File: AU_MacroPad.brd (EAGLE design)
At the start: 59.7 x 104.1 mm, 96 parts, among them IC1 74HCT1G125DBV, IC3 RP2040_QFN56, SW2 RA SW, SW3 EN11-VSM1AF15, U1 W25Q64, U2 RT9080-3.3, U3 PAM8302, X1 TYPE C, X2 ZJY130-2864KSWLG22, Y1 12MHz/12pF

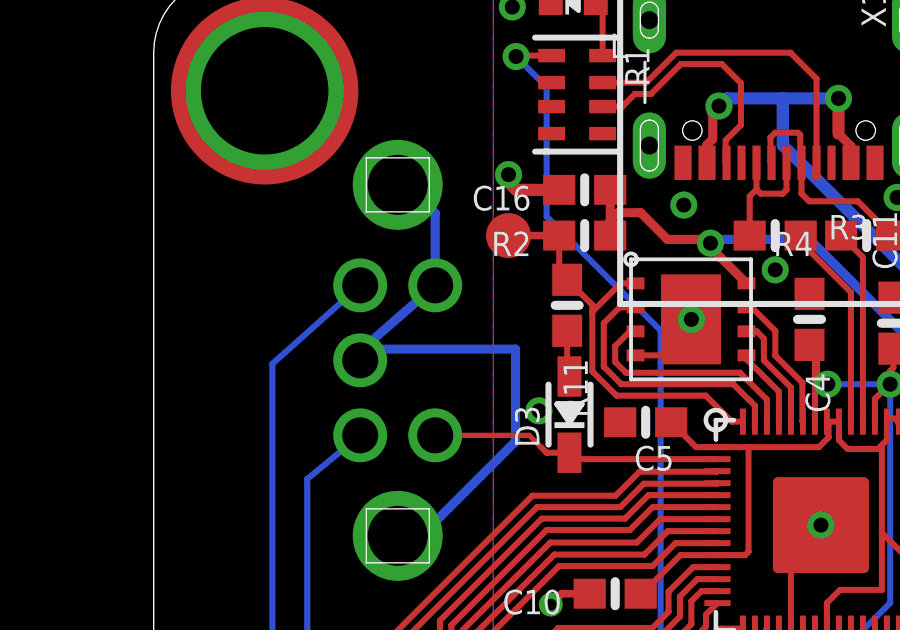
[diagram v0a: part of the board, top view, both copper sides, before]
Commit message: swap gnd and usbboot to match original macropad
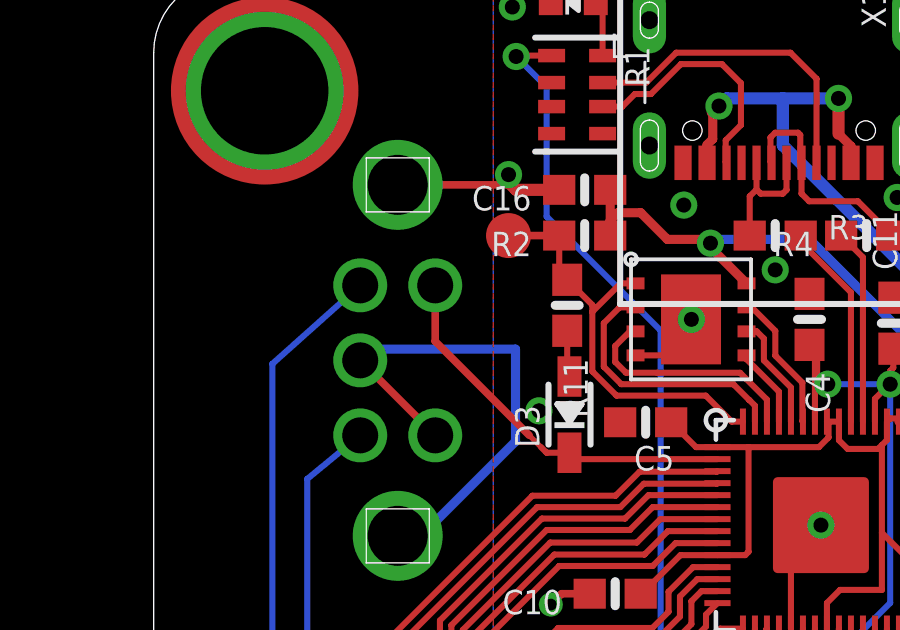
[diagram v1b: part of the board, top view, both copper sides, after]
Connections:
- net GND: now also SW3.D; no longer SW3.E
- net USBBOOT: now also SW3.E; no longer SW3.D
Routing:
- net USBBOOT: track 9.84 -> 13.0 mm
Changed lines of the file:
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@@
 <via x="51.308" y="79.121" extent="1-16" drill="0.5"/>
 <via x="36.114896875" y="96.474196875" extent="1-16" drill="0.5"/>
-<contactref element="SW3" pad="E"/>
 <contactref element="SW3" pad="P$2"/>
 <contactref element="SW3" pad="P$1"/>
 <contactref element="SW3" pad="C"/>
-<wire x1="17.1342" y1="97.1947" x2="18.38424375" y2="96.256228125" width="0.3048" layer="16"/>
-<wire x1="18.38424375" y1="96.256228125" x2="18.3842" y2="93.8447" width="0.3048" layer="16"/>
-<wire x1="18.3842" y1="93.8447" x2="15.946940625" y2="91.718925" width="0.3048" layer="16"/>
 <wire x1="15.893640625" y1="91.665625" x2="15.8842" y2="91.3447" width="0.3048" layer="16"/>
 <wire x1="17.1342" y1="85.4947" x2="18.226859375" y2="85.806228125" width="0.3048" layer="16"/>
@@
 <contactref element="C18" pad="1"/>
 <contactref element="C30" pad="1"/>
+<contactref element="SW3" pad="D"/>
+<wire x1="18.3842" y1="88.8447" x2="15.8842" y2="91.3447" width="0.254" layer="1"/>
+<wire x1="17.1342" y1="97.1947" x2="20.9153" y2="97.1947" width="0.254" layer="1"/>
+<wire x1="20.9153" y1="97.1947" x2="21.082" y2="97.028" width="0.254" layer="1"/>
 </signal>
 <signal name="MISO">
@@
 <wire x1="21.908478125" y1="88.454521875" x2="22.098" y2="88.265" width="0.2032" layer="1"/>
 <wire x1="22.098" y1="88.265" x2="22.86" y2="88.265" width="0.2032" layer="1"/>
-<contactref element="SW3" pad="D"/>
-<wire x1="18.3842" y1="88.8447" x2="21.5183" y2="88.8447" width="0.1778" layer="1"/>
-<wire x1="21.5183" y1="88.8447" x2="21.908478125" y2="88.454521875" width="0.1778" layer="1"/>
+<wire x1="21.908478125" y1="88.454521875" x2="21.5183" y2="88.8447" width="0.1778" layer="1"/>
+<contactref element="SW3" pad="E"/>
+<wire x1="21.5183" y1="88.8447" x2="18.3842" y2="91.9788" width="0.254" layer="1"/>
+<wire x1="18.3842" y1="91.9788" x2="18.3842" y2="93.8447" width="0.254" layer="1"/>
 </signal>
 <signal name="N$4">

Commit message: add bottom fiducials, clean up silk due to other side OLED
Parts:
- added U$79, U$83: FIDUCIAL_1MM, microbuilder:FIDUCIAL_1MM
- X2: value ZJY130-2864KSWLG22 -> ZJY130-2864KSWLG22_CONN; device adafruit_display:ZJY130-2864KSWLG22 -> adafruit_display:ZJY130-2864KSWLG22_JUSTCONN
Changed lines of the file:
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@@
 <grid distance="0.003329" unitdist="inch" unit="inch" style="lines" multiple="1" display="yes" altdistance="0.025" altunitdist="inch" altunit="inch"/>
 <layers>
-<layer number="1" name="Top" color="4" fill="1" visible="yes" active="yes"/>
+<layer number="1" name="Top" color="4" fill="1" visible="no" active="yes"/>
 <layer number="2" name="Route2" color="16" fill="3" visible="no" active="no"/>
 <layer number="3" name="Route3" color="17" fill="3" visible="no" active="no"/>
@@
 <layer number="14" name="Route14" color="22" fill="6" visible="no" active="no"/>
 <layer number="15" name="Route15" color="23" fill="6" visible="no" active="no"/>
-<layer number="16" name="Bottom" color="1" fill="1" visible="yes" active="yes"/>
+<layer number="16" name="Bottom" color="1" fill="1" visible="no" active="yes"/>
 <layer number="17" name="Pads" color="2" fill="1" visible="yes" active="yes"/>
 <layer number="18" name="Vias" color="2" fill="1" visible="yes" active="yes"/>
@@
 <layer number="20" name="Dimension" color="24" fill="1" visible="yes" active="yes"/>
 <layer number="21" name="tPlace" color="7" fill="1" visible="no" active="yes"/>
-<layer number="22" name="bPlace" color="7" fill="1" visible="no" active="yes"/>
-<layer number="23" name="tOrigins" color="15" fill="1" visible="yes" active="yes"/>
-<layer number="24" name="bOrigins" color="15" fill="1" visible="no" active="yes"/>
+<layer number="22" name="bPlace" color="7" fill="1" visible="yes" active="yes"/>
+<layer number="23" name="tOrigins" color="15" fill="1" visible="no" active="yes"/>
+<layer number="24" name="bOrigins" color="15" fill="1" visible="yes" active="yes"/>
 <layer number="25" name="tNames" color="7" fill="1" visible="no" active="yes"/>
 <layer number="26" name="bNames" color="7" fill="1" visible="no" active="yes"/>
-<layer number="27" name="tValues" color="7" fill="1" visible="yes" active="yes"/>
+<layer number="27" name="tValues" color="7" fill="1" visible="no" active="yes"/>
 <layer number="28" name="bValues" color="7" fill="1" visible="no" active="yes"/>
 <layer number="29" name="tStop" color="7" fill="3" visible="no" active="yes"/>
-<layer number="30" name="bStop" color="7" fill="6" visible="no" active="yes"/>
+<layer number="30" name="bStop" color="7" fill="6" visible="yes" active="yes"/>
 <layer number="31" name="tCream" color="7" fill="4" visible="no" active="yes"/>
 <layer number="32" name="bCream" color="7" fill="5" visible="no" active="yes"/>
@@
 <layer number="44" name="Drills" color="7" fill="1" visible="no" active="yes"/>
 <layer number="45" name="Holes" color="7" fill="1" visible="no" active="yes"/>
-<layer number="46" name="Milling" color="3" fill="1" visible="yes" active="yes"/>
+<layer number="46" name="Milling" color="3" fill="1" visible="no" active="yes"/>
 <layer number="47" name="Measures" color="7" fill="1" visible="no" active="yes"/>
 <layer number="48" name="Document" color="7" fill="1" visible="no" active="yes"/>
@@
 <layer number="199" name="Contour" color="7" fill="1" visible="no" active="yes"/>
 <layer number="200" name="BackSilk" color="7" fill="10" visible="no" active="yes"/>
-<layer number="201" name="FrontSilk" color="7" fill="10" visible="no" active="yes"/>
+<layer number="201" name="FrontSilk" color="7" fill="10" visible="yes" active="yes"/>
 <layer number="202" name="202bmp" color="3" fill="10" visible="no" active="yes"/>
 <layer number="203" name="203bmp" color="4" fill="10" visible="no" active="yes"/>
@@
 <attribute name="FORCETHM" value="1" x="55.88" y="100.33" size="1.778" layer="27" display="off"/>
 </element>
-<element name="X2" library="adafruit_display" package="ZJY130-2864KSWLG22" value="ZJY130-2864KSWLG22" x="41.799078125" y="97.0858875" smashed="yes">
+<element name="X2" library="adafruit_display" package="ZJY130-2864KSWLG22_JUSTCONN" value="ZJY130-2864KSWLG22_CONN" x="41.799078125" y="97.0858875" smashed="yes">
 <attribute name="NAME" x="24.899078125" y="107.9358875" size="0.8128" layer="25" ratio="18"/>
 <attribute name="ROT" value="180" x="41.799078125" y="97.0858875" size="1.778" layer="27" display="off"/>
@@
 <attribute name="VALUE" x="35.176534375" y="61.137059375" size="0.4064" layer="27" ratio="10" rot="R90"/>
 </element>
+<element name="U$79" library="microbuilder" package="FIDUCIAL_1MM" value="FIDUCIAL_1MM" x="50.733959375" y="101.80614375" smashed="yes" rot="MR0">
+<attribute name="BOM" value="EXCLUDE" x="50.733959375" y="101.80614375" size="1.778" layer="28" rot="MR0" display="off"/>
+</element>
+<element name="U$83" library="microbuilder" package="FIDUCIAL_1MM" value="FIDUCIAL_1MM" x="28.15735" y="88.53075625" smashed="yes" rot="MR0">
+<attribute name="BOM" value="EXCLUDE" x="28.15735" y="88.53075625" size="1.778" layer="28" rot="MR0" display="off"/>
+</element>
 </elements>

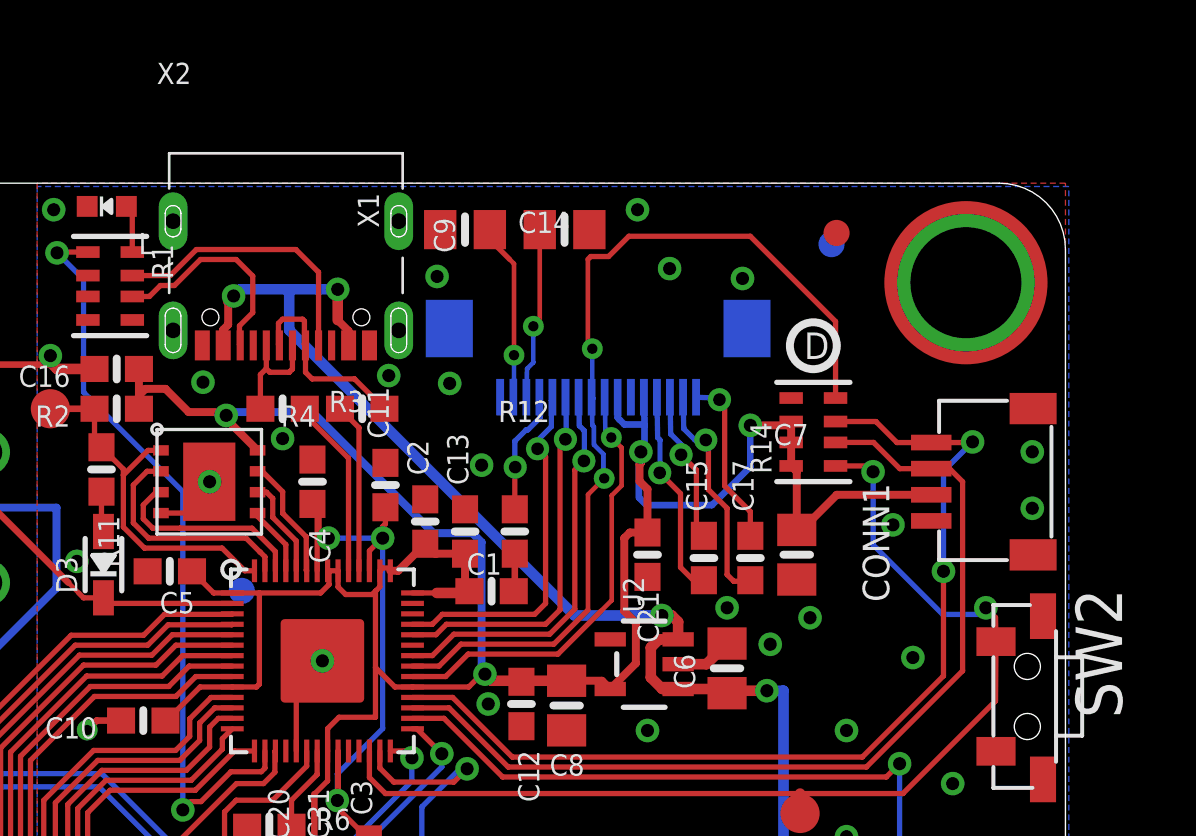
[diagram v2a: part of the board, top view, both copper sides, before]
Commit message: rotated connector
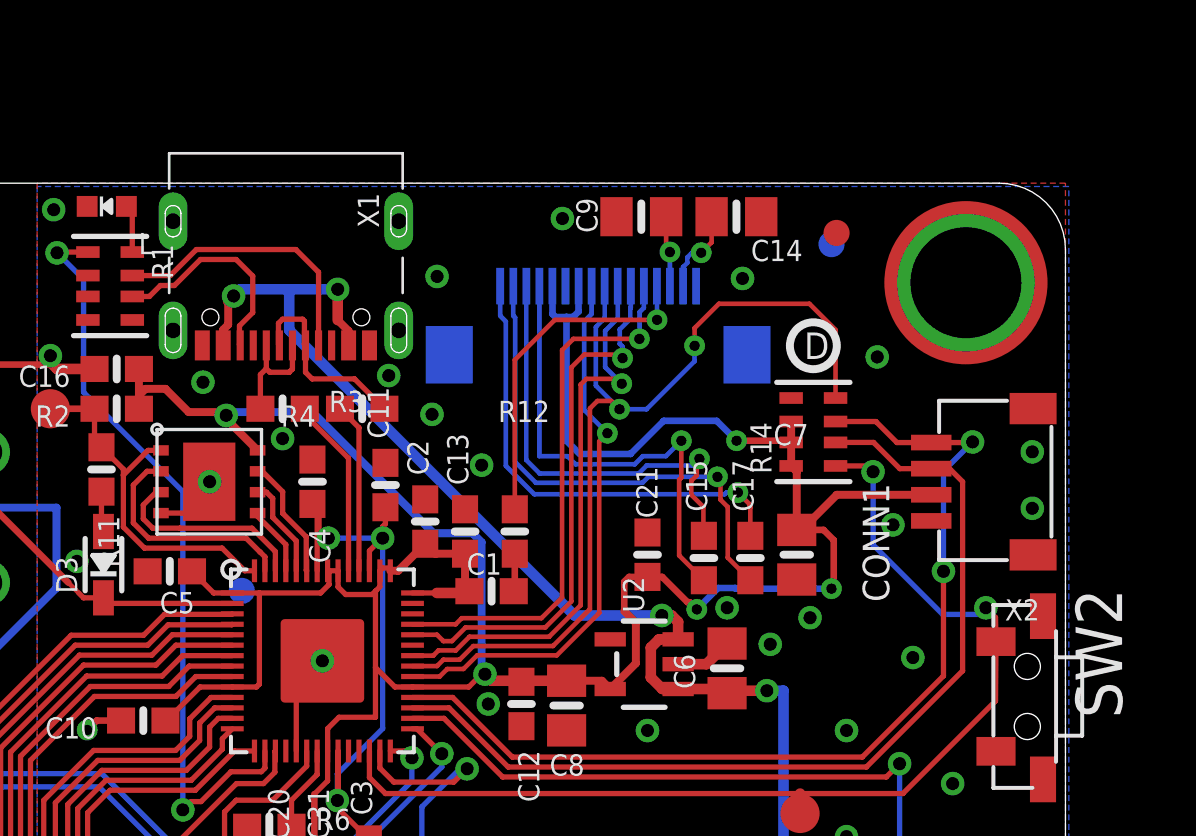
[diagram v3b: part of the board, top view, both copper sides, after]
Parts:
- moved C14 10.4 mm to (47.1, 102.9), turned to 180 degrees
- moved C9 2.98 mm to (43.5, 102.9), turned to 0 degrees
- moved X2 1.97 mm to (41.8, 99.1), turned to 180 degrees
- turned C21 to 270 degrees
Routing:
- net N$24: track 6.62 -> 18.2 mm
- net N$26: track 5.83 -> 17.0 mm
- net N$23: track 8.73 -> 19.4 mm
- net N$25: track 7.99 -> 18.2 mm
- net 3.3V: track 106.8 -> 116.8 mm, vias 4 -> 5
- net N$21: track 4.74 -> 13.1 mm
- net MOSI: track 13.7 -> 20.9 mm
- net SCK: track 14.3 -> 21.0 mm
- net OLED_DC: track 15.3 -> 21.6 mm
- net OLED_CS: track 17.0 -> 21.3 mm
- net VCOMH: track 6.62 -> 2.72 mm
- net VCC: track 6.88 -> 3.32 mm
